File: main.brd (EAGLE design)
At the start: 78.8 x 63 mm, 8 parts, among them X1 FH12-40S-0.5SH

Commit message: button expansion
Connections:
- removed net LEDSCL: BUTTONS.4
- removed net N$22: U$1.19/A5/SCL
- removed net N$23: U$1.18/A4/SDA
- removed net N$3: U$1.2
- removed net N$4: U$1.3/CANTX
- removed net N$5: U$1.4/CANRX
- new net LED_SCL: BUTTONS.4, U$1.19/A5/SCL
- new net N$1: U$1.5
- net BUTTON_CLK: now also U$1.3/CANTX
- net BUTTON_DATA: now also U$1.4/CANRX
- net BUTTON_S/P: now also U$1.2
- net LED_SDA: now also U$1.18/A4/SDA
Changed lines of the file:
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@@
 <signal name="LED_SDA">
 <contactref element="BUTTONS" pad="3"/>
+<contactref element="U$1" pad="18/A4/SDA"/>
+<wire x1="6.35" y1="57.15" x2="24.13" y2="43.18" width="0" layer="19" extent="1-1"/>
 </signal>
 <signal name="BUTTON_S/P">
 <contactref element="BUTTONS" pad="5"/>
+<contactref element="U$1" pad="2"/>
+<wire x1="11.43" y1="27.94" x2="8.89" y2="57.15" width="0" layer="19" extent="1-1"/>
 </signal>
 <signal name="BUTTON_CLK">
 <contactref element="BUTTONS" pad="7"/>
+<contactref element="U$1" pad="3/CANTX"/>
+<wire x1="13.97" y1="27.94" x2="11.43" y2="57.15" width="0" layer="19" extent="1-1"/>
 </signal>
-<signal name="LEDSCL">
+<signal name="LED_SCL">
 <contactref element="BUTTONS" pad="4"/>
+<contactref element="U$1" pad="19/A5/SCL"/>
+<wire x1="21.59" y1="43.18" x2="6.35" y2="59.69" width="0" layer="19" extent="1-1"/>
 </signal>
 <signal name="BUTTON_DATA">
 <contactref element="BUTTONS" pad="6"/>
+<contactref element="U$1" pad="4/CANRX"/>
+<wire x1="16.51" y1="27.94" x2="8.89" y2="59.69" width="0" layer="19" extent="1-1"/>
 </signal>
 <signal name="SPI_CS">
@@
 <signal name="+12V">
 <contactref element="GENERAL_XPN" pad="3"/>
-</signal>
-<signal name="N$3">
-<contactref element="U$1" pad="2"/>
-</signal>
-<signal name="N$4">
-<contactref element="U$1" pad="3/CANTX"/>
-</signal>
-<signal name="N$5">
-<contactref element="U$1" pad="4/CANRX"/>
 </signal>
 <signal name="N$6">
@@
 <contactref element="U$1" pad="20/A6"/>
 </signal>
-<signal name="N$22">
-<contactref element="U$1" pad="19/A5/SCL"/>
-</signal>
-<signal name="N$23">
-<contactref element="U$1" pad="18/A4/SDA"/>
-</signal>
 <signal name="N$24">
 <contactref element="U$1" pad="17/A3"/>
@@
 <contactref element="U$1" pad="39/A20"/>
 </signal>
+<signal name="N$1">
+<contactref element="U$1" pad="5"/>
+</signal>
 </signals>

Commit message: Milestone fully drafted
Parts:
- removed AUDIO_MAIN: (no value), pinhead:1X03
- removed KNOBBOARD: (no value), con-dil:IC14PL
- removed SOUND_MOD_XPN: (no value), pinhead:2X04
- removed X1: FH12-40S-0.5SH, con-hirose:FH12-40S-0.5SH
- added AUDIO_OUT: (no value), SparkFun-Connectors:1X03
- added J1: (no value), SparkFun-Connectors:2X8
- added SCR: FH12-40S-0.5SH, con-hirose:FH12-40S-0.5SH
- added SOUND_MODS: (no value), SparkFun-Connectors:2X4
- BUTTONS: device pinhead:2X04 -> SparkFun-Connectors:2X4
- GENERAL_XPN: device pinhead:2X05 -> SparkFun-Connectors:2X5
- PORTBOARD: device con-dil:IC24PL -> SparkFun-Connectors:2X13
- moved GENERAL_XPN 27.1 mm to (16.5, 31.8)
- moved BUTTONS 25.4 mm to (7.62, 33.0)
- moved PORTBOARD 17.0 mm to (3.81, 3.81), turned to 0 degrees
- moved U$1 16.5 mm to (31.8, 19.1)
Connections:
- removed net N$13: U$1.28
- removed net N$14: U$1.29
- removed net N$15: U$1.30
- removed net N$18: U$1.23/A9
- removed net N$19: U$1.22/A8
- removed net N$24: U$1.17/A3
- removed net N$30: U$1.35/A16
- removed net N$31: U$1.36/A17
- removed net N$32: U$1.37/A18
- removed net N$33: U$1.38/A19
- removed net N$34: U$1.39/A20
- new net USBDATA+: PORTBOARD.13
- new net USBDATA-: PORTBOARD.14
- net +12V: now also PORTBOARD.26
- net +3V3: now also J1.1, PORTBOARD.2, SCR.2; no longer KNOBBOARD.1, PORTBOARD.24, X1.2
- net +5V: now also PORTBOARD.4; no longer PORTBOARD.23
- net AUDIO_GND: now also AUDIO_OUT.2; no longer AUDIO_MAIN.2
- net AUDIO_L: now also AUDIO_OUT.1; no longer AUDIO_MAIN.1
- net AUDIO_R: now also AUDIO_OUT.3; no longer AUDIO_MAIN.3
- net GND: now also J1.2, PORTBOARD.3, SCR.1; no longer KNOBBOARD.14, PORTBOARD.2, X1.1
- net JOYSTICK_B: now also J1.14, U$1.17/A3; no longer KNOBBOARD.8
- net JOYSTICK_X: now also J1.11, U$1.23/A9; no longer KNOBBOARD.6
- net JOYSTICK_Y: now also J1.13, U$1.22/A8; no longer KNOBBOARD.7
- net MIDIIN1: now also PORTBOARD.6; no longer PORTBOARD.22
- net MIDIIN2: now also PORTBOARD.8; no longer PORTBOARD.21
- net MIDIIN3: now also PORTBOARD.10; no longer PORTBOARD.20
- net MIDIIN4: now also PORTBOARD.12; no longer PORTBOARD.19
- net MIDIOUT1: now also PORTBOARD.5; no longer PORTBOARD.3
- net MIDIOUT2: now also PORTBOARD.7; no longer PORTBOARD.4
- net MIDIOUT3: now also PORTBOARD.9; no longer PORTBOARD.5
- net MIDIOUT4: now also PORTBOARD.11; no longer PORTBOARD.6
- net ROTENC1_A: now also J1.3, U$1.28; no longer KNOBBOARD.2
- net ROTENC1_B: now also J1.5, U$1.29; no longer KNOBBOARD.3
- net ROTENC2_A: now also J1.7, U$1.30; no longer KNOBBOARD.4
- net ROTENC2_B: now also J1.9, U$1.39/A20; no longer KNOBBOARD.5
- net ROTENC3_A: now also J1.4, U$1.38/A19; no longer KNOBBOARD.13
- net ROTENC3_B: now also J1.6, U$1.37/A18; no longer KNOBBOARD.12
- net ROTENC4_A: now also J1.8, U$1.36/A17; no longer KNOBBOARD.11
- net ROTENC4_B: now also J1.10, U$1.35/A16; no longer KNOBBOARD.10
- net SCR_BL: now also SCR.29; no longer X1.29
- net SCR_CLK: now also SCR.24; no longer X1.24
- net SCR_CS: now also SCR.23; no longer X1.23
- net SCR_DC: now also SCR.25; no longer X1.25
- net SCR_MOSI: now also SCR.27; no longer X1.27
- net SCR_MOSO: now also SCR.28; no longer X1.28
- net SDCLK: now also PORTBOARD.19; no longer PORTBOARD.9
- net SDCMD: now also PORTBOARD.20; no longer PORTBOARD.16
- net SDDATA0: now also PORTBOARD.15; no longer PORTBOARD.7
- net SDDATA1: now also PORTBOARD.16; no longer PORTBOARD.18
- net SDDATA2: now also PORTBOARD.17; no longer PORTBOARD.8
- net SDDATA3: now also PORTBOARD.18; no longer PORTBOARD.17
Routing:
- net +3V3: track 0.00 -> 108.3 mm, vias 0 -> 1
- net MIDIIN4: track 0.00 -> 86.0 mm
- net MIDIOUT4: track 0.00 -> 73.1 mm, vias 0 -> 1
- net SCR_DC: track 0.00 -> 63.2 mm, vias 0 -> 1
- net MIDIIN3: track 0.00 -> 58.1 mm, vias 0 -> 1
- net MIDIOUT3: track 0.00 -> 56.9 mm
- net JOYSTICK_X: track 0.00 -> 53.9 mm
- net JOYSTICK_Y: track 0.00 -> 52.6 mm
- net AUDIO_GND: track 0.00 -> 46.5 mm, vias 0 -> 1
- net +5V: track 0.00 -> 45.8 mm
- net SCR_BL: track 0.00 -> 43.2 mm, vias 0 -> 1
- net SCR_MOSO: track 0.00 -> 41.7 mm, vias 0 -> 2
- net AUDIO_R: track 0.00 -> 41.0 mm
- net SCR_CS: track 0.00 -> 39.9 mm
- net JOYSTICK_B: track 0.00 -> 38.9 mm, vias 0 -> 1
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- added copper zone on layer 1, net GND
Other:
- board size 78.8 x 63 mm -> 74.9 x 37.6 mm

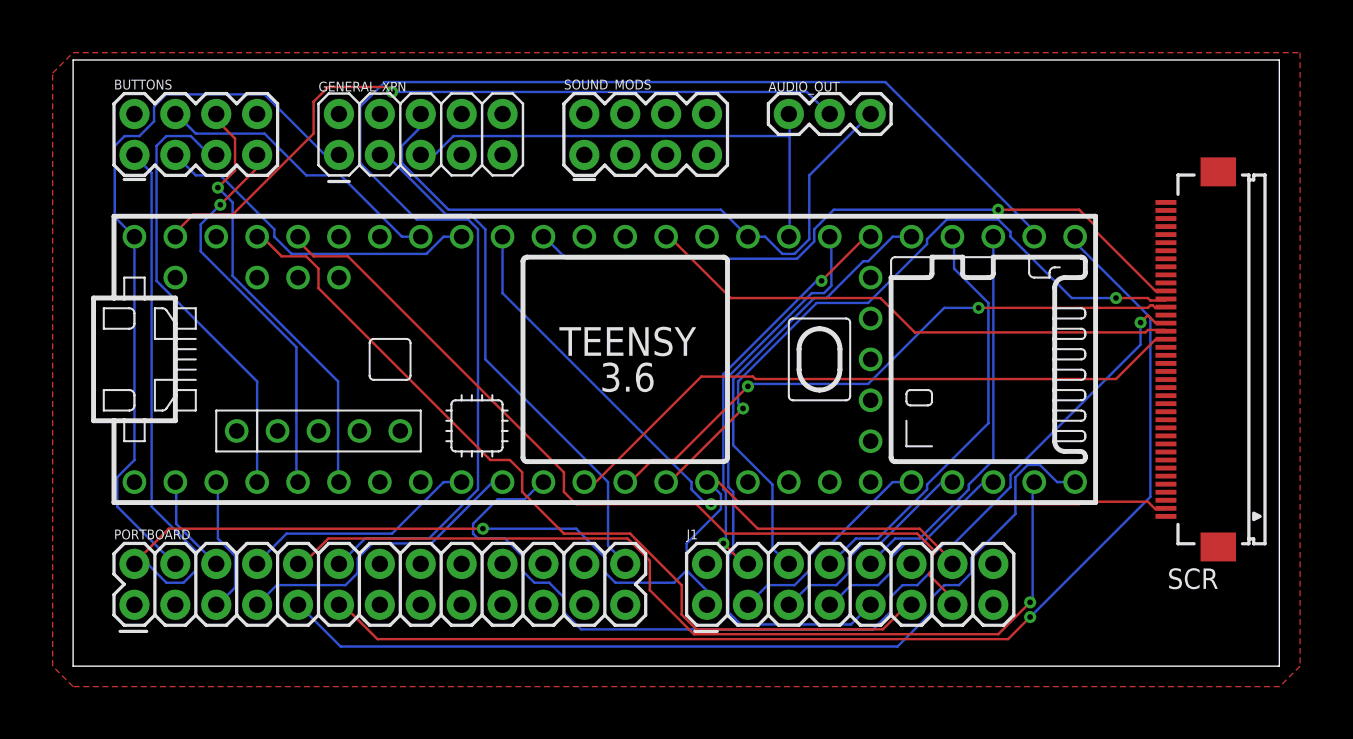
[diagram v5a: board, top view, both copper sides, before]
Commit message: KNOBBOARD pinout fixed, seperate audio ground added, pinhead lib switched to, pcb rerouted. TODO general expansion and mixing
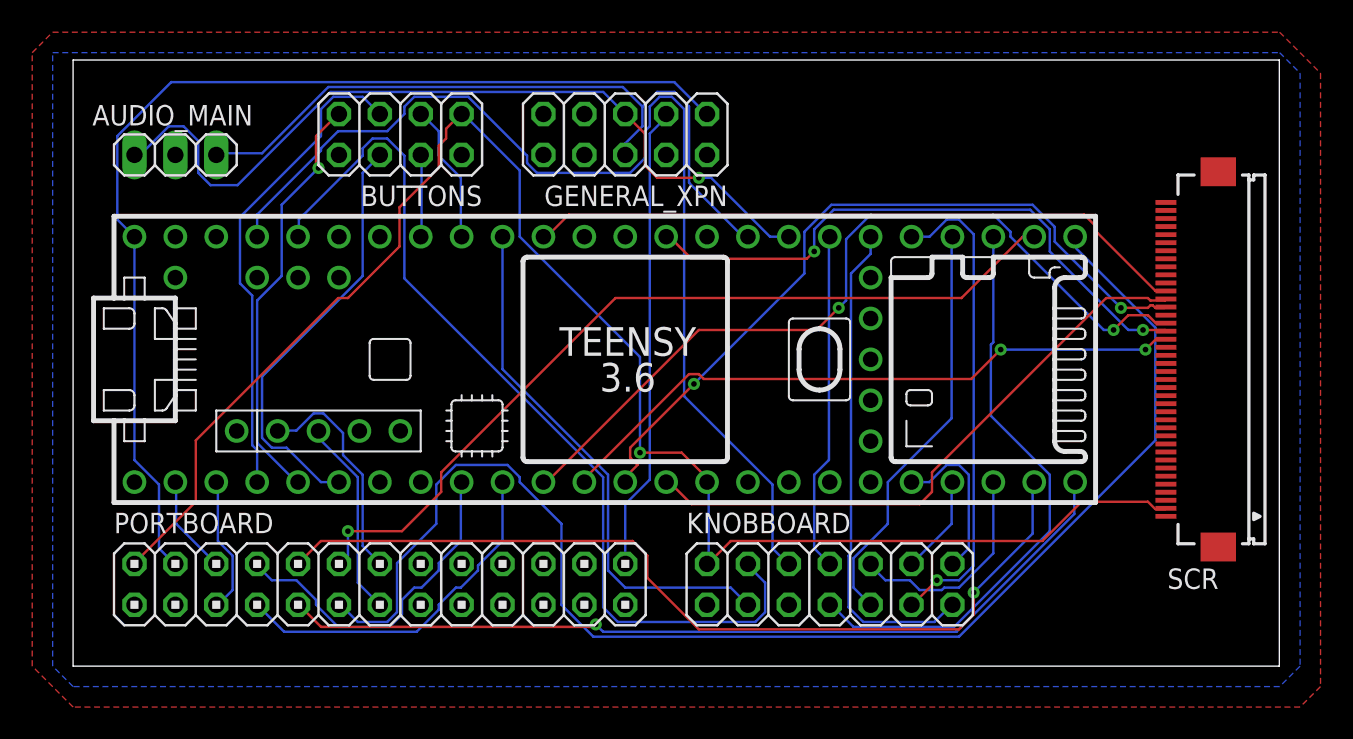
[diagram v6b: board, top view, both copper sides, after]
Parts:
- removed AUDIO_OUT: (no value), SparkFun-Connectors:1X03
- removed J1: (no value), SparkFun-Connectors:2X8
- removed SOUND_MODS: (no value), SparkFun-Connectors:2X4
- added AUDIO_MAIN: (no value), pinhead:1X03
- added KNOBBOARD: (no value), pinhead:2X07
- BUTTONS: device SparkFun-Connectors:2X4 -> pinhead:2X04
- GENERAL_XPN: device SparkFun-Connectors:2X5 -> pinhead:2X05
- PORTBOARD: device SparkFun-Connectors:2X13 -> pinhead:2X13
- moved GENERAL_XPN 17.8 mm to (34.3, 33.0), turned to 180 degrees
- moved PORTBOARD 15.3 mm to (19.1, 5.08)
- moved BUTTONS 12.7 mm to (20.3, 33.0), turned to 180 degrees
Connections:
- removed net AUDIO_GND: AUDIO_OUT.2, U$1.AGND
- new net AGND: AUDIO_MAIN.2
- net +3V3: now also KNOBBOARD.13; no longer J1.1
- net AUDIO_L: now also AUDIO_MAIN.1; no longer AUDIO_OUT.1
- net AUDIO_R: now also AUDIO_MAIN.3; no longer AUDIO_OUT.3
- net GND: now also KNOBBOARD.14; no longer J1.2
- net JOYSTICK_B: now also KNOBBOARD.12; no longer J1.14
- net JOYSTICK_X: now also KNOBBOARD.9; no longer J1.11
- net JOYSTICK_Y: now also KNOBBOARD.11; no longer J1.13
- net ROTENC1_A: now also KNOBBOARD.1; no longer J1.3
- net ROTENC1_B: now also KNOBBOARD.3; no longer J1.5
- net ROTENC2_A: now also KNOBBOARD.5; no longer J1.7
- net ROTENC2_B: now also KNOBBOARD.7; no longer J1.9
- net ROTENC3_A: now also KNOBBOARD.2; no longer J1.4
- net ROTENC3_B: now also KNOBBOARD.4; no longer J1.6
- net ROTENC4_A: now also KNOBBOARD.6; no longer J1.8
- net ROTENC4_B: now also KNOBBOARD.8; no longer J1.10
- net USBDATA+: now also U$1.UD+
- net USBDATA-: now also U$1.UD-
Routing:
- net AUDIO_GND: track 46.5 -> 0.00 mm, vias 1 -> 0
- net MIDIIN4: track 86.0 -> 53.2 mm, vias 0 -> 1
- net +5V: track 45.8 -> 66.9 mm
- net AUDIO_L: track 31.1 -> 51.4 mm, vias 0 -> 1
- net ROTENC2_B: track 36.4 -> 21.1 mm
- net JOYSTICK_X: track 53.9 -> 68.4 mm
- net USBDATA-: track 0.00 -> 14.1 mm
- net LED_SCL: track 18.4 -> 5.15 mm
- net MIDIOUT4: track 73.1 -> 85.8 mm, vias 1 -> 0
- net USBDATA+: track 0.00 -> 12.4 mm
- net LED_SDA: track 21.0 -> 8.73 mm
- net ROTENC4_B: track 24.4 -> 36.6 mm
- net SCR_DC: track 63.2 -> 51.5 mm, vias 1 -> 2
- net SCR_MOSI: track 38.2 -> 47.0 mm
- net ROTENC1_B: track 13.9 -> 6.16 mm
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- added copper zone on layer 16, net AGND

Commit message: PDFs of sch & brd
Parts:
- turned GENERAL_XPN to 0 degrees
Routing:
- net MIDIOUT4: track 85.8 -> 57.0 mm, vias 0 -> 2
- net JOYSTICK_X: track 68.4 -> 46.9 mm
- net MIDIIN4: track 53.2 -> 74.4 mm
- net JOYSTICK_Y: track 57.7 -> 40.7 mm
- net +5V: track 66.9 -> 53.3 mm
- net ROTENC4_A: track 25.9 -> 35.5 mm
- net SCR_DC: track 51.5 -> 61.1 mm, vias 2 -> 0
- net MIDIIN2: track 21.2 -> 15.0 mm
- net AUDIO_R: track 45.6 -> 39.6 mm
- net ROTENC1_B: track 6.16 -> 11.0 mm
- net SCR_CS: track 40.2 -> 44.8 mm, vias 2 -> 1
- net SCR_CLK: track 37.6 -> 33.5 mm, vias 2 -> 0
- net BUTTON_DATA: track 26.5 -> 22.4 mm
- net ROTENC1_A: track 10.2 -> 6.16 mm
- net MIDIIN3: track 55.9 -> 51.8 mm, vias 1 -> 3
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
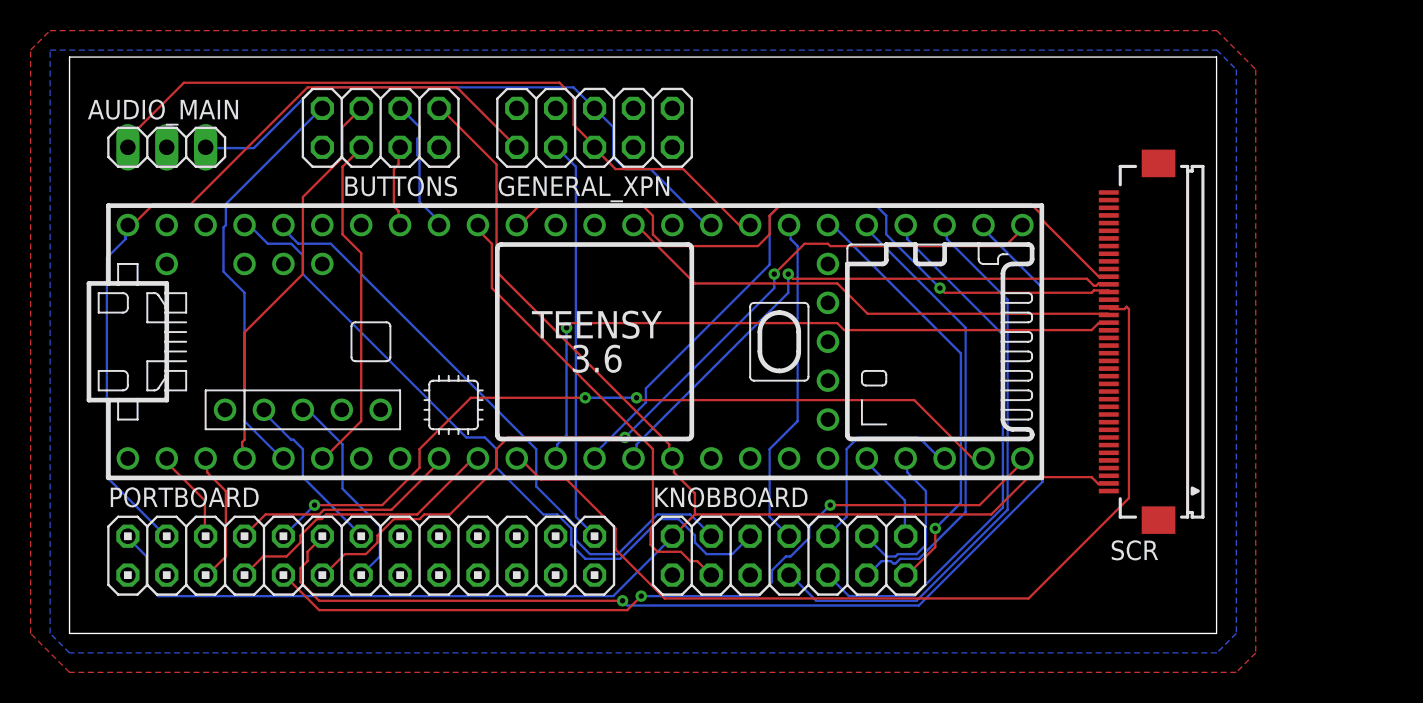
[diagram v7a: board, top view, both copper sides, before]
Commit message: xpn-SPI connected, portboard audio added
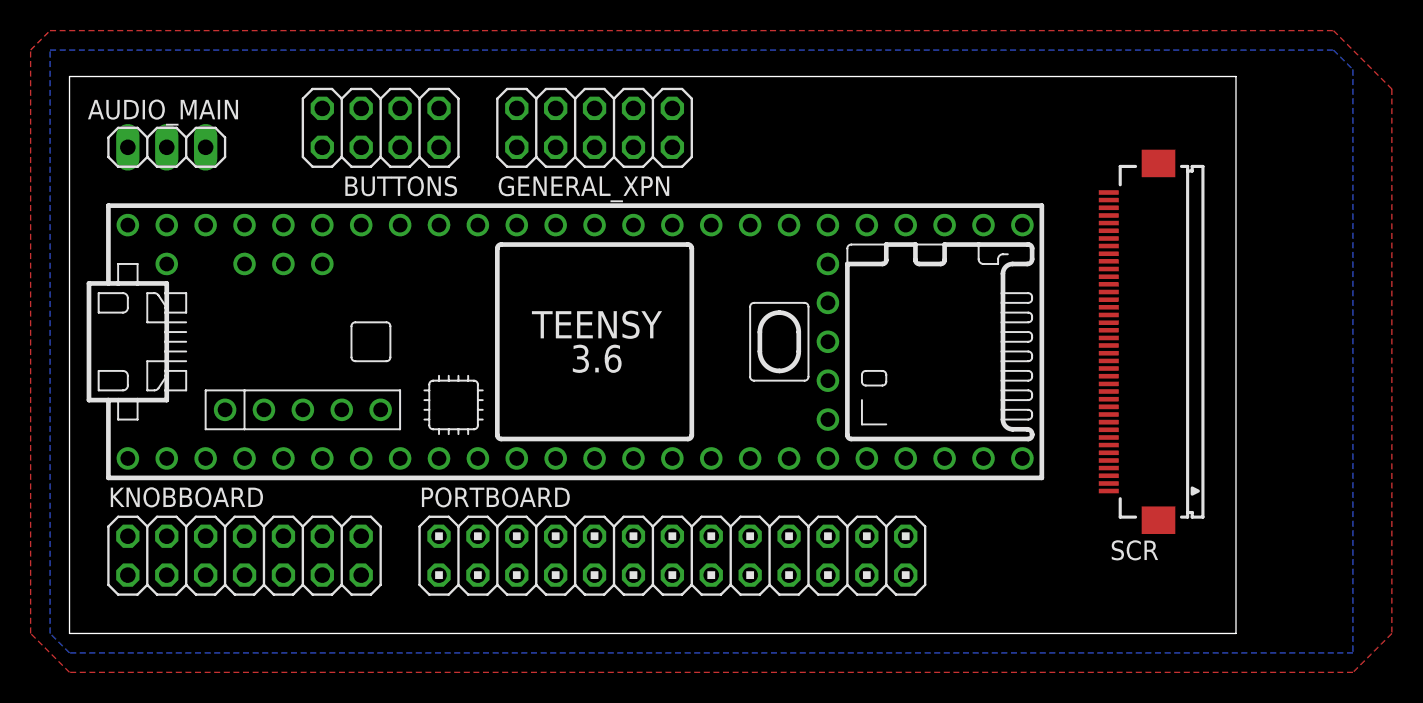
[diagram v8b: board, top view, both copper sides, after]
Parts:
- moved KNOBBOARD 35.6 mm to (11.4, 5.08)
- moved PORTBOARD 20.3 mm to (39.4, 5.08)
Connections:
- removed net N$1: U$1.5
- removed net N$20: U$1.21/A7
- removed net N$21: U$1.20/A6
- net AGND: now also PORTBOARD.25
- net AUDIO_L: now also PORTBOARD.23
- net AUDIO_R: now also PORTBOARD.24
- net JOYSTICK_B: now also KNOBBOARD.10; no longer KNOBBOARD.12
- net SPI_CLK: now also U$1.20/A6
- net SPI_MISO: now also U$1.5
- net SPI_MOSI: now also U$1.21/A7
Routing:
- net +3V3: track 103.8 -> 0.00 mm
- net MIDIIN4: track 74.4 -> 0.00 mm, vias 1 -> 0
- net SCR_DC: track 61.1 -> 0.00 mm
- net MIDIOUT4: track 57.0 -> 0.00 mm, vias 2 -> 0
- net MIDIOUT3: track 54.4 -> 0.00 mm, vias 2 -> 0
- net +5V: track 53.3 -> 0.00 mm
- net MIDIIN3: track 51.8 -> 0.00 mm, vias 3 -> 0
- net AUDIO_L: track 47.7 -> 0.00 mm
- net JOYSTICK_X: track 46.9 -> 0.00 mm
- net SCR_MOSI: track 46.3 -> 0.00 mm, vias 1 -> 0
- net SCR_BL: track 45.1 -> 0.00 mm
- net SCR_CS: track 44.8 -> 0.00 mm, vias 1 -> 0
- net JOYSTICK_Y: track 40.7 -> 0.00 mm
- net AUDIO_R: track 39.6 -> 0.00 mm
- net ROTENC4_B: track 37.7 -> 0.00 mm
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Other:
- board size 74.9 x 37.6 mm -> 76.2 x 36.4 mm
